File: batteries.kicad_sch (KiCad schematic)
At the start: 46 parts, among them J19 61300311121, J3 67996-110HLF, J5 Conn_01x04_Socket, Q26 EPC2016C, Q27 EPC2016C, Q8 SI2302DDS-T1-GE3, U30 LTC3833EUDC-TRPBF

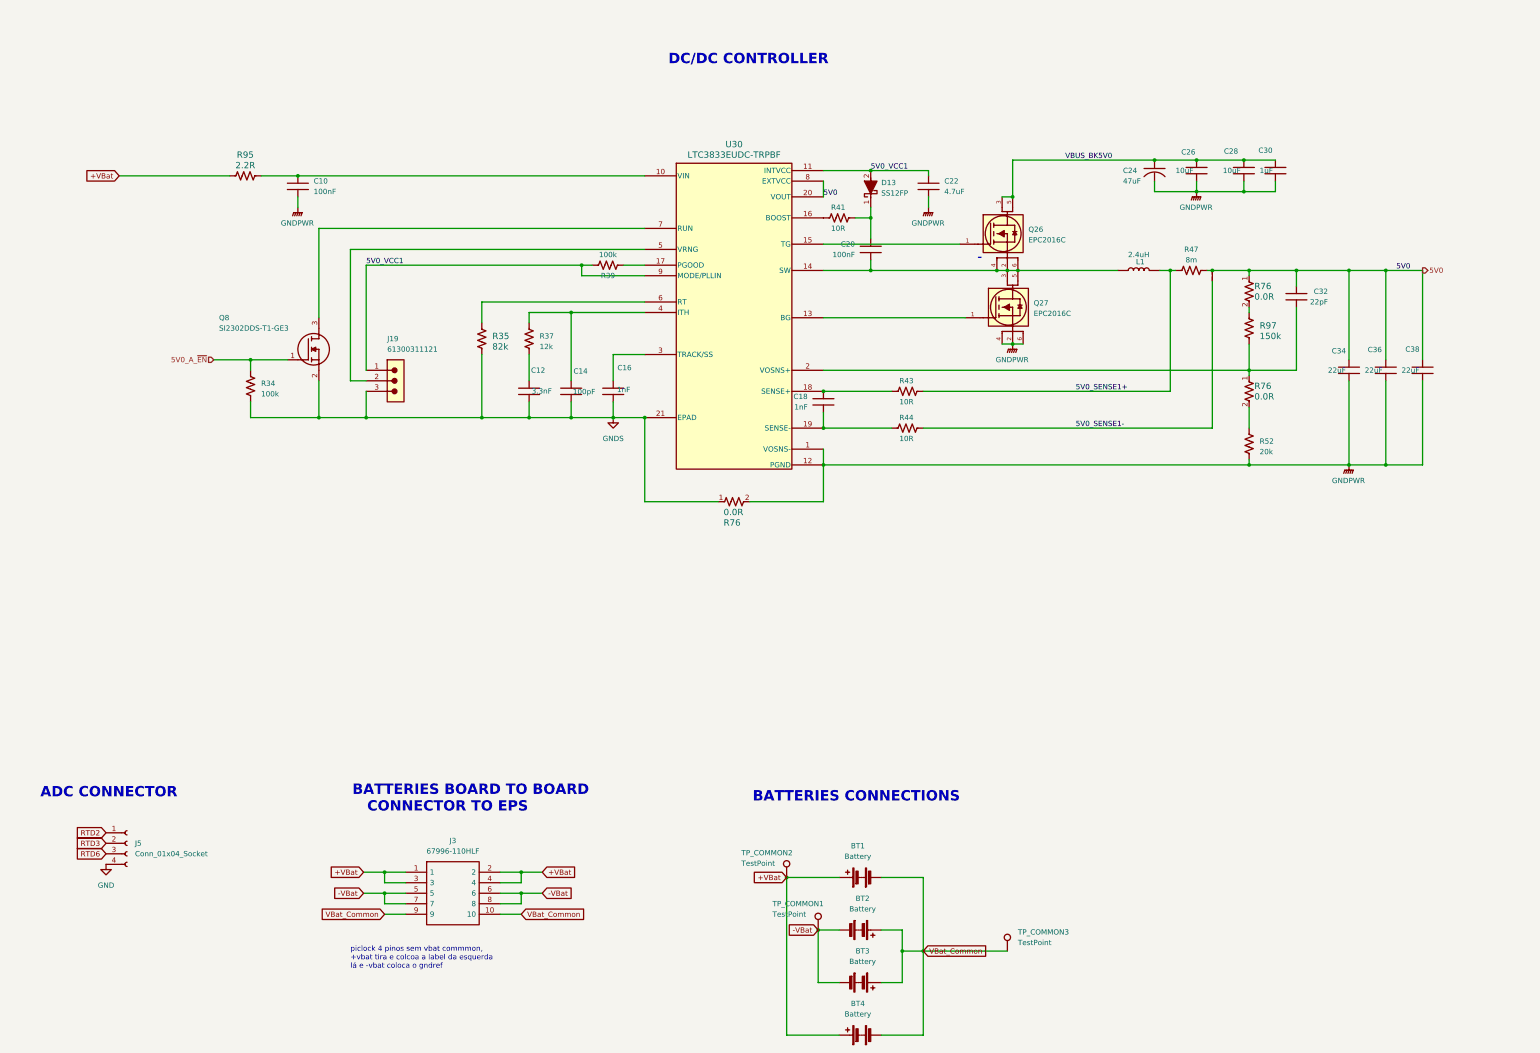
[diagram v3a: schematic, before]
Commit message: Creating hierarquical labels and organizing root
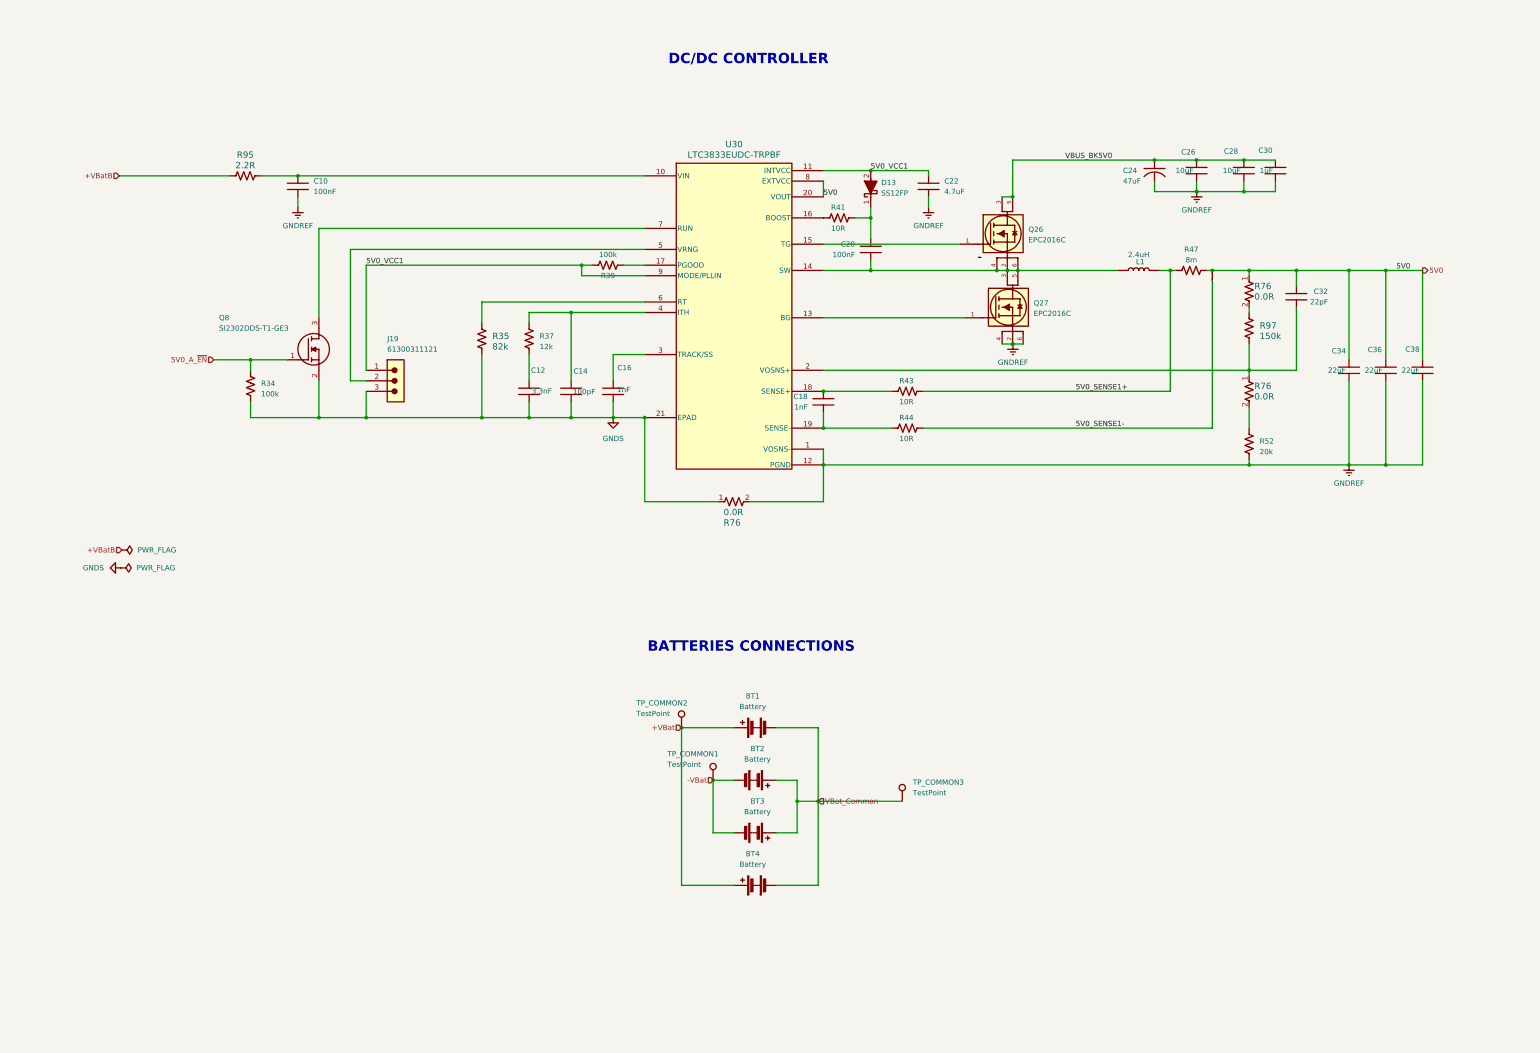
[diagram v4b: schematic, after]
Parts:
- removed J3: 67996-110HLF, lib:67996-110HLF, symbol 67996-110HLF:67996-110HLF
- removed J5: Conn_01x04_Socket, symbol Connector:Conn_01x04_Socket
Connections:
- net +VBat: no longer R95.2
- net GNDPWR renamed GNDREF
- new net +VBatB: R95.2
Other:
- note removed: "ADC CONNECTOR"
- note removed: "BATTERIES BOARD TO BOARD CONNECTOR TO EPS"
- note removed: "piclock 4 pinos sem vbat commmon, +vbat tira e colcoa a label da esquerda lá e -vbat coloca o gndref"
- moved on the sheet: BT1, BT2, BT3, BT4, TP_COMMON1, TP_COMMON2, TP_COMMON3

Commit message: general improvements in schematics
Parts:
- removed J19: 61300311121, footprints:three_position_jumper, symbol 61300311121:61300311121
- removed L1: 2.4uH, footprints:744325240, symbol 744325240:744325240
- removed Q26, Q27: EPC2016C, footprints:EPC2016C, symbol EPC2016C:EPC2016C
- removed Q8: SI2302DDS-T1-GE3, footprints:SI2302DDS-T1-GE3, symbol SI2302DDS-T1-GE3:SI2302DDS-T1-GE3
- removed R35: 82k, footprints:CRCW060382K0FKEA, symbol CRCW060382K0FKEA:CRCW060382K0FKEA
- removed R41, R43, R44: 10R, footprints:CRCW060310R0FKEAHP, symbol CRCW060310R0FKEAHP:CRCW060310R0FKEAHP
- removed R76 (x3): 0.0R, footprints:CRCW06030000Z0EAHP, symbol CRCW06030000Z0EAHP:CRCW06030000Z0EAHP
- removed R95: 2.2R, footprints:CRCW06032R20FKEAHP, symbol CRCW06032R20FKEAHP:CRCW06032R20FKEAHP
- removed R97: 150k, footprints:CRCW0603150KFKEAHP, symbol CRCW0603150KFKEAHP:CRCW0603150KFKEAHP
- added J23: 61300311121, footprints:61300311121, symbol 61300311121:61300311121
- added L2: 2.4uH, footprints:744325240, symbol 744325240:744325240
- added Q28, Q30: EPC2016C, footprints:EPC2016C, symbol EPC2016C:EPC2016C
- added Q9: SI2302DDS-T1-GE3, footprints:SI2302DDS-T1-GE3, symbol SI2302DDS-T1-GE3:SI2302DDS-T1-GE3
- added R41 (x3): 10R, Resistor_SMD:R_0603_1608Metric_Pad0.98x0.95mm_HandSolder, symbol CRCW060310R0FKEAHP:CRCW060310R0FKEAHP
- added R50: 90.9k, Resistor_SMD:R_0603_1608Metric_Pad0.98x0.95mm_HandSolder, symbol CRCW060390K9FKEAHP:CRCW060390K9FKEAHP
- added R76 (x3): 0.0R, Resistor_SMD:R_0603_1608Metric_Pad0.98x0.95mm_HandSolder, symbol CRCW06030000Z0EAHP:CRCW06030000Z0EAHP
- added R96: 2.2R, Resistor_SMD:R_0603_1608Metric_Pad0.98x0.95mm_HandSolder, symbol CRCW06032R20FKEAHP:CRCW06032R20FKEAHP
- added R97: 82k, Resistor_SMD:R_0603_1608Metric_Pad0.98x0.95mm_HandSolder, symbol CRCW060382K0FKEA:CRCW060382K0FKEA
- BT1, BT2, BT3, BT4: footprint (none) -> footprints:BATTERY_18650_STRIP_CONTACT
- C10, C20: footprint footprints:C0603C104K5RACTU -> Capacitor_SMD:C_0603_1608Metric_Pad1.08x0.95mm_HandSolder
- C12: footprint footprints:C0603C332J5GACAUTO -> Capacitor_SMD:C_0603_1608Metric_Pad1.08x0.95mm_HandSolder
- C14: footprint footprints:C0603C101J5GACAUTO -> Capacitor_SMD:C_0603_1608Metric_Pad1.08x0.95mm_HandSolder
- C16, C18: footprint footprints:C0603C102F3GACTU -> Capacitor_SMD:C_0603_1608Metric_Pad1.08x0.95mm_HandSolder
- C22: footprint footprints:GCM32ER71H475KA55L -> Capacitor_SMD:C_0603_1608Metric_Pad1.08x0.95mm_HandSolder
- C24: footprint footprints:T495X476K035ATE300 -> Capacitor_SMD:C_0603_1608Metric_Pad1.08x0.95mm_HandSolder
- C26, C28: footprint footprints:C1210C106K5RACTU -> Capacitor_SMD:C_0603_1608Metric_Pad1.08x0.95mm_HandSolder
- C30: footprint footprints:C0805C105K5RACTU -> Capacitor_SMD:C_0603_1608Metric_Pad1.08x0.95mm_HandSolder
- C32: footprint footprints:C0603C220K5RACAUTO -> Capacitor_SMD:C_0603_1608Metric_Pad1.08x0.95mm_HandSolder
- C34, C36, C38: footprint footprints:GCM32ER71C226KE19L -> Capacitor_SMD:C_0603_1608Metric_Pad1.08x0.95mm_HandSolder
- R34, R39: footprint footprints:CRCW0603100KFKEAHP -> Resistor_SMD:R_0603_1608Metric_Pad0.98x0.95mm_HandSolder
- R37: footprint footprints:CRCW060312K0FKEAHP -> Resistor_SMD:R_0603_1608Metric_Pad0.98x0.95mm_HandSolder
- R47: footprint footprints:WSL20108L000FEA18 -> Resistor_SMD:R_2010_5025Metric_Pad1.40x2.65mm_HandSolder
- R52: footprint footprints:CRCW060320K0FKEAHP -> Resistor_SMD:R_0603_1608Metric_Pad0.98x0.95mm_HandSolder
- TP_COMMON1, TP_COMMON2, TP_COMMON3: footprint (none) -> TestPoint:TestPoint_Pad_D2.5mm
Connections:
- net +VBatB: now also R96.2
- net GNDREF: now also Q30.2 (Substrate), Q30.4 (Source), Q30.6 (Source), R76.2
- net GNDS: now also J23.3, Q9.2 (S), R76.1, R97.1
- net at C10.2, U30.10 (VIN): now also R96.1
- net at U30.13 (BG): now also Q30.1 (Gate)
- net at C20.2, U30.14 (SW): now also L2.1, Q28.2 (Substrate), Q28.4 (Source), Q28.6 (Source), Q30.3 (Drain), Q30.5 (Drain)
- net at U30.15 (TG): now also Q28.1 (Gate)
- net at U30.16 (BOOST): now also R41.2
- net at C18.1, U30.18 (SENSE+): now also R41.2
- net at C18.2, U30.19 (SENSE-): now also R41.2
- net at C32.2, U30.2 (VOSNS+): now also R50.1, R76.1
- net at C14.1, U30.4 (ITH): now also R37.1; no longer R37.2
- net at U30.5 (VRNG): now also J23.2
- net at U30.6 (RT): now also R97.2
- net at U30.7 (RUN): now also Q9.3 (D)
- net at R52.2: now also R76.2
- net at C20.1, D13.1 (K): now also R41.1
- net at C12.1: now also R37.2; no longer R37.1
- net 5V0 renamed 3V3
- net 3V3: now also R76.1
- net 5V0_A_~{EN} renamed 3V3_A_~{EN}
- net 3V3_A_~{EN}: now also Q9.1 (G)
- net 5V0_SENSE1+ renamed 3V3_SENSE1+
- net 3V3_SENSE1+: now also L2.2, R41.1
- net 5V0_SENSE1- renamed 3V3_SENSE1-
- net 3V3_SENSE1-: now also R41.1
- net 5V0_VCC1 renamed 3V3_VCC1
- net 3V3_VCC1: now also J23.1
- net VBUS_BK5V0 renamed VBUS_BK3V3
- net VBUS_BK3V3: now also Q28.3 (Drain), Q28.5 (Drain)
- new net: R50.2, R76.2
